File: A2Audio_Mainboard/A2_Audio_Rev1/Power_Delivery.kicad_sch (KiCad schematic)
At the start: 93 parts, among them J1 USB_C_Receptacle, U1 USBLC6-2SC6, U13 LT3042xMSE, U14 W25Q16JVSS, U19 TPS62130, U2 TPS65987DDHRSHR, U21 TPS61230DRC, U24 TPS65131RGE, U25 LT3094xDD, U3 TUSB546A-DCIRNQR, U4 BQ25895RTWR, U5 MAX17055ETB_T

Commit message: Added footprints and a few more parts.
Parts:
- C1, C19, C2, C20, C21, C22, C3, C38, C4, C42, C43, C44, C45, C47, C48, C49, C5, C50, C51, C52, C53, C54, C55, C56, C57, C6, C64, C65, C66, C67, C68, C69, C70, C71, C84, C85, C86, C87, C88, C89, C90, C92: footprint (none) -> Capacitor_SMD:C_0402_1005Metric
- D1: footprint (none) -> LED_SMD:LED_0603_1608Metric
- R1, R11, R12, R13, R14, R15, R16, R17, R18, R19, R2, R20, R21, R22, R23, R24, R25, R27, R28, R3, R31, R32, R33, R34, R35, R36, R4, R5, R6, R9: footprint (none) -> Resistor_SMD:R_0402_1005Metric
- TH1: footprint (none) -> Resistor_SMD:R_0603_1608Metric

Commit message: More Refinement
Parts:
- added J4: 12401610E4_2A, custom:AMPHENOL_12401610E4_2A, symbol 12401610E4_2A:12401610E4_2A
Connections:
- net CC1: now also J4.A5 (CC1)
- net CC2: now also J4.B5 (CC2)
- net D+1: now reaches J1.A6 (D+), J1.B6 (D+), U1.3 (I/O2)
- net D-1: now reaches J1.A7 (D-), J1.B7 (D-), U1.1 (I/O1)
- net TYPEC_RX1_N renamed RX1-1
- net TYPEC_RX1_P renamed RX1+1
- net VBUS_RAW renamed VBUS_A
- net VBUS_A: now also J4.A4 (VBUS_A), J4.A9 (VBUS_A), J4.B4 (VBUS_B), J4.B9 (VBUS_B)
- new net: J4.SH1 (SHIELD), J4.SH2 (SHIELD), J4.SH3 (SHIELD), J4.SH4 (SHIELD)
- new net GND_A: J4.A1 (GND_A), J4.A12 (GND_A)
- new net GND_B: J4.B1 (GND_B), J4.B12 (GND_B)

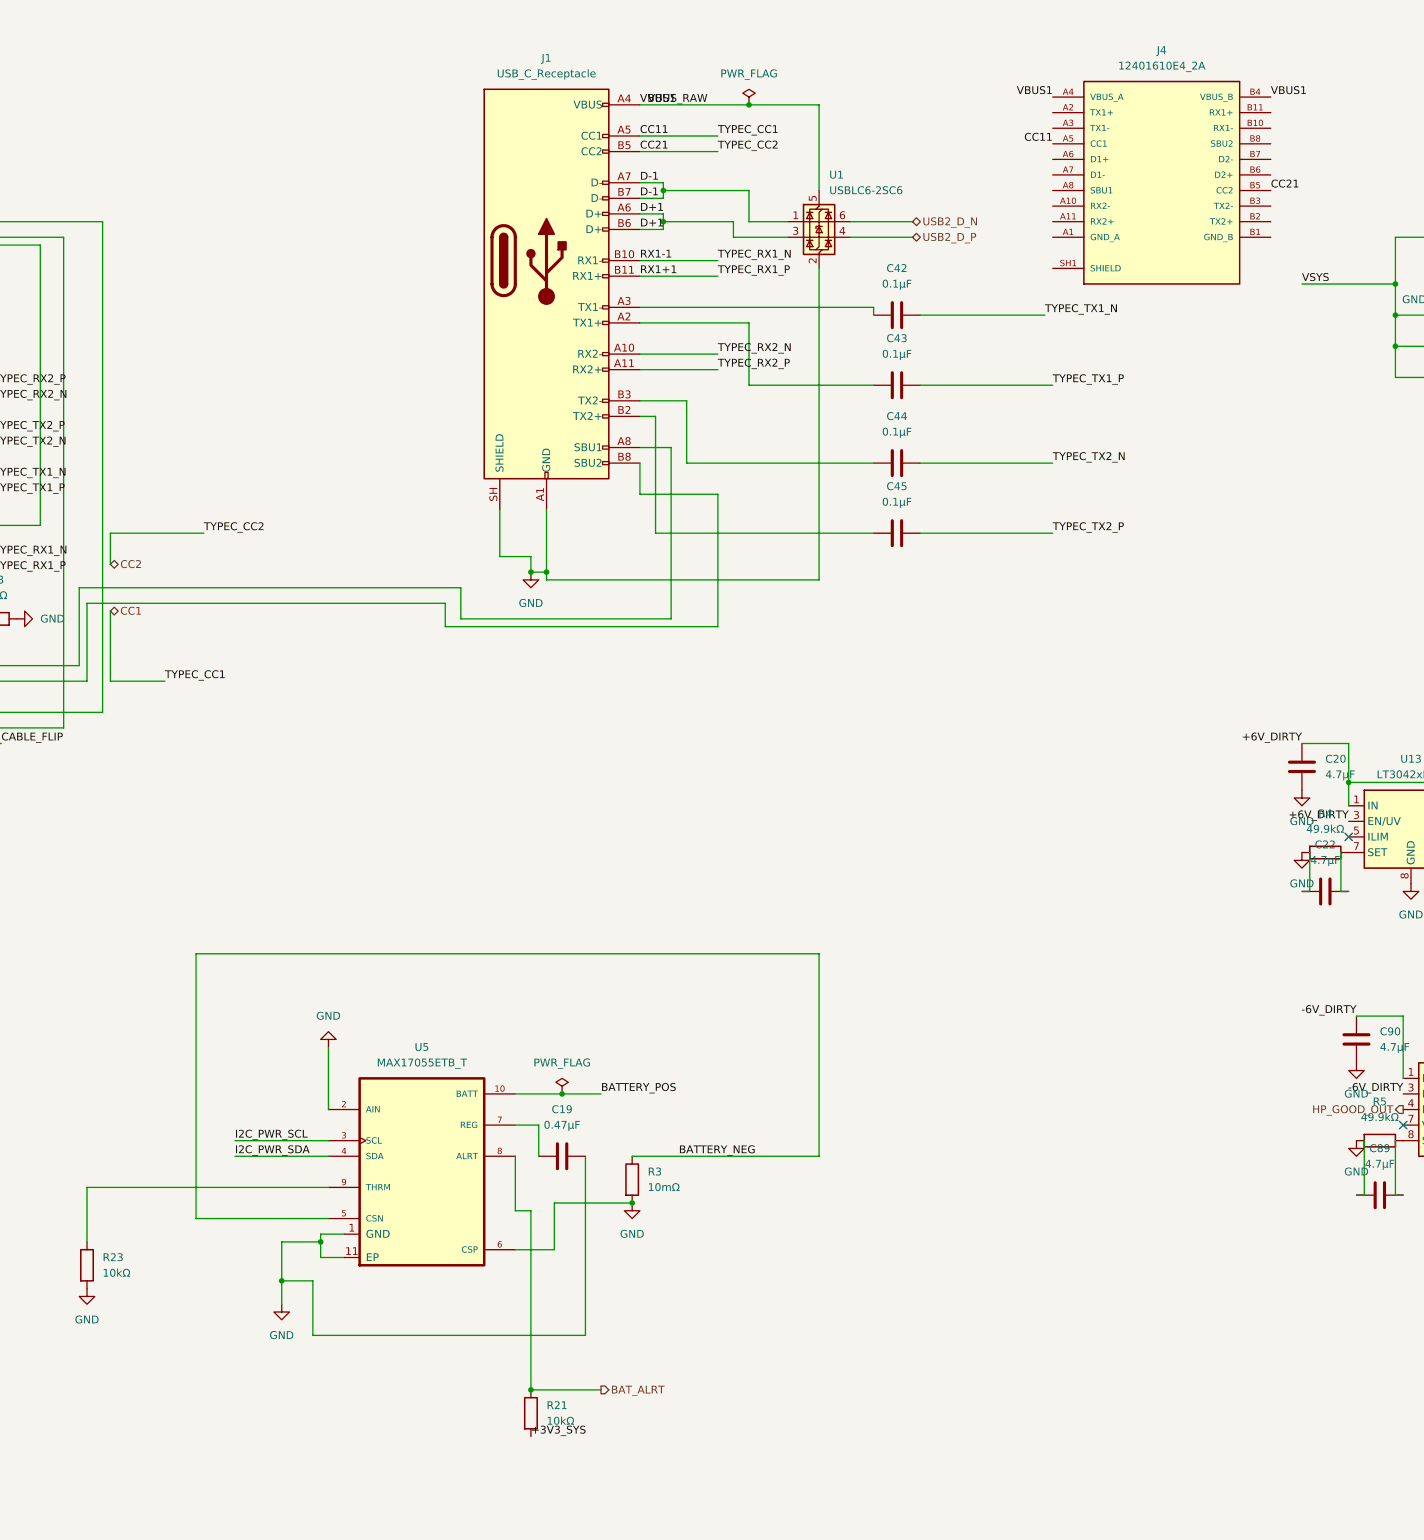
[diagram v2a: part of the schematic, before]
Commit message: Refining of logic and adding battery connector
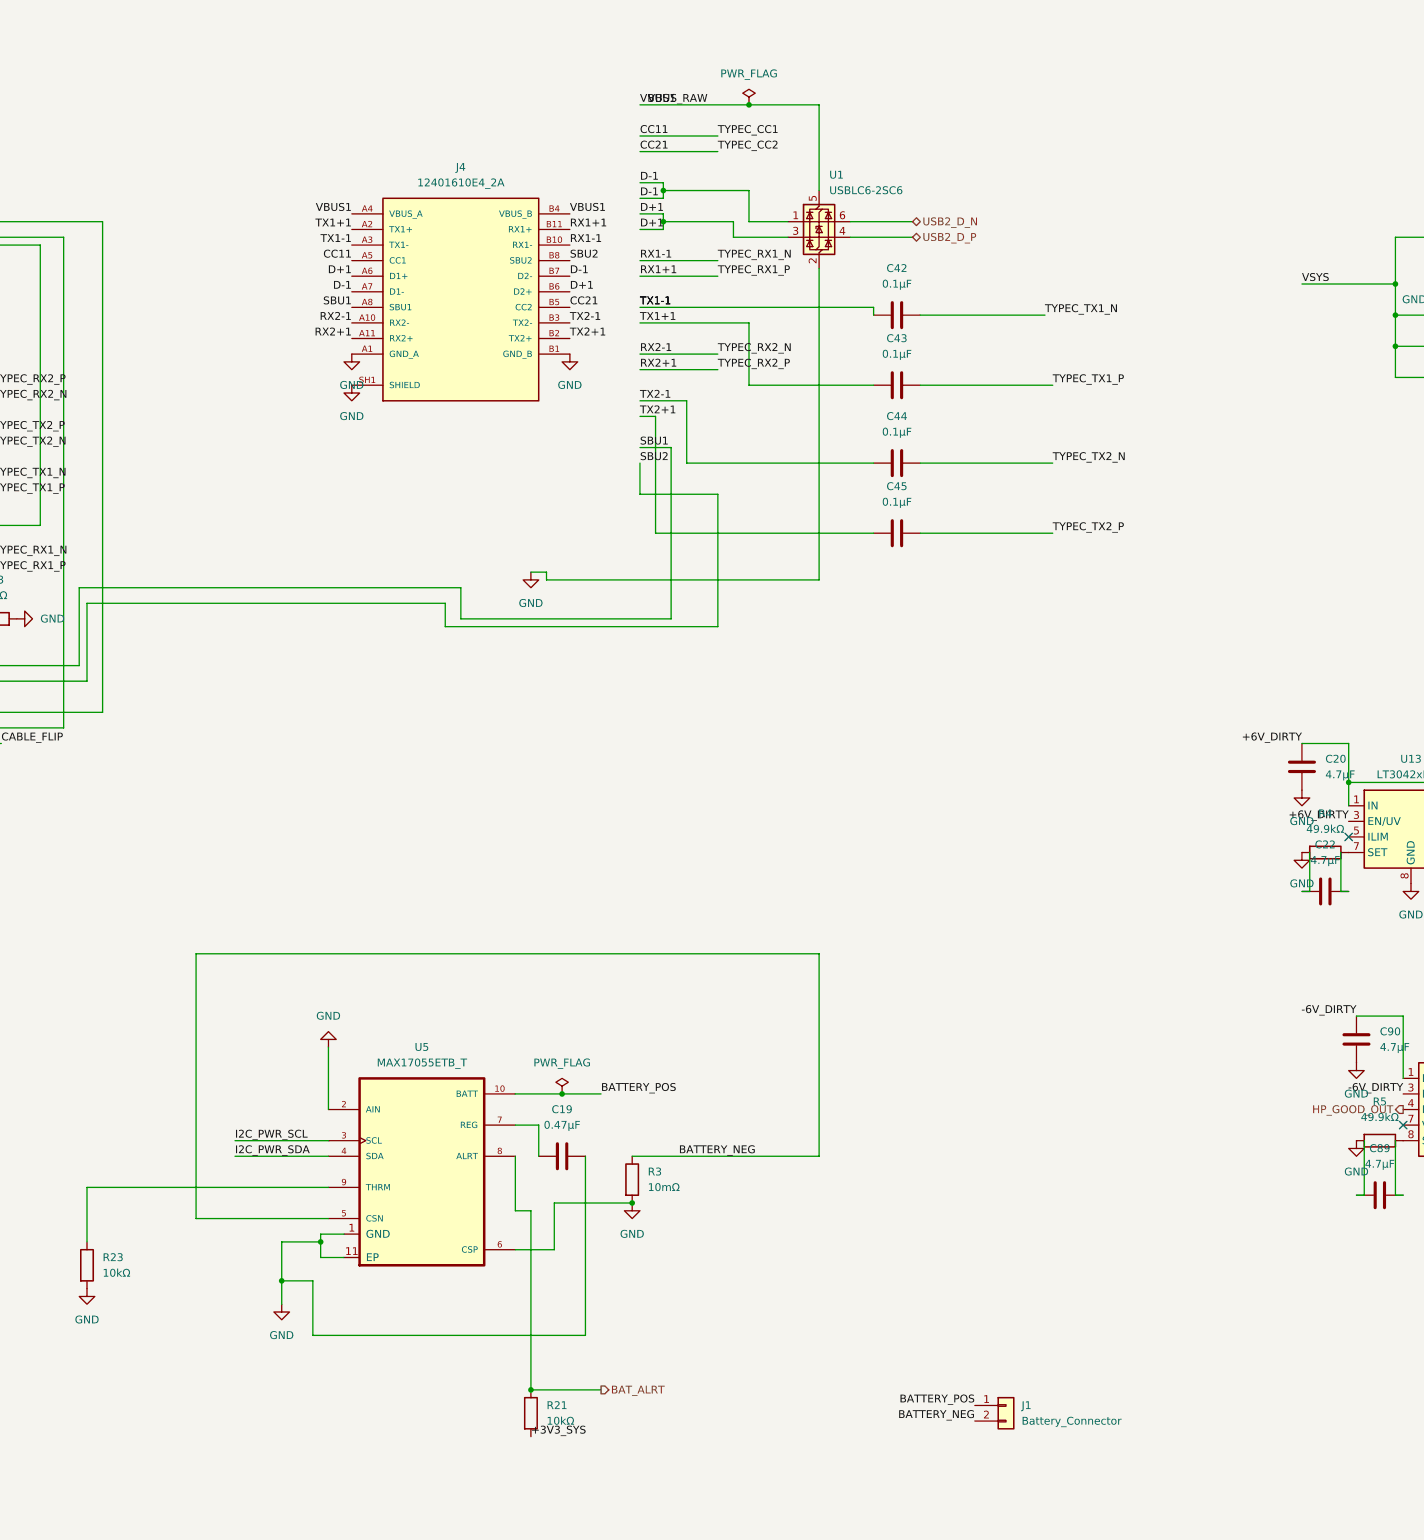
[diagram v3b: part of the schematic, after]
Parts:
- removed J1: USB_C_Receptacle, symbol symbols:USB_C_Receptacle
- added J1: Battery_Connector, Connector_JST:JST_PH_S2B-PH-K_1x02_P2.00mm_Horizontal, symbol symbols:Conn_01x02
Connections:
- net GND_A is gone; now on net CSP: J4.A1 (GND_A), J4.A12 (GND_A)
- net GND_B is gone; now on net CSP: J4.B1 (GND_B), J4.B12 (GND_B)
- net TYPEC_RX2_N is gone; now on net RX2-1: U3.39 (RX2N)
- net TYPEC_RX2_P is gone; now on net RX2+1: U3.40 (RX2P)
- net BAT: now also J1.1 (Pin_1)
- net BATTERY_NEG: now also J1.2 (Pin_2)
- net CSP: now also J4.SH1 (SHIELD), J4.SH2 (SHIELD), J4.SH3 (SHIELD), J4.SH4 (SHIELD)
- net D+1: now also J4.A6 (D1+), J4.B6 (D2+)
- net D-1: now also J4.A7 (D1-), J4.B7 (D2-)
- net RX1+1: now also J4.B11 (RX1+)
- net RX1-1: now also J4.B10 (RX1-)
- net TX2-1: now reaches C44.1
- net TX2-1: now also J4.B3 (TX2-)
- net RX2-1: now reaches J4.A10 (RX2-)
- net RX2+1: now reaches J4.A11 (RX2+)
- net TX1+1: now reaches J4.A2 (TX1+)
- net TX1+1: now also C43.1
- net TX1-1: now reaches J4.A3 (TX1-)
- net TX1-1: now also C42.1
- net SBU1: now reaches J4.A8 (SBU1)
- net SBU1: now also U3.27 (SBU1)
- net TX2+1: now reaches J4.B2 (TX2+)
- net TX2+1: now also C45.1
- net SBU2: now reaches J4.B8 (SBU2)
- net SBU2: now also U3.26 (SBU2)
- net CC1 renamed CC11
- net CC2 renamed CC21
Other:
- moved on the sheet: J4

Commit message: Fixing ERC errors
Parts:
- removed C64, C65, C66, C67, C68, C69, C70, C71: 100nF, Capacitor_SMD:C_0402_1005Metric, symbol symbols:C
- removed C85: 22µF, Capacitor_SMD:C_0402_1005Metric, symbol symbols:C
- removed C86: 0.22µF, Capacitor_SMD:C_0402_1005Metric, symbol symbols:C
- removed R19: 100kΩ, Resistor_SMD:R_0402_1005Metric, symbol symbols:R
- removed R31: 1MΩ, Resistor_SMD:R_0402_1005Metric, symbol symbols:R
- removed R32: 255kΩ, Resistor_SMD:R_0402_1005Metric, symbol symbols:R
- removed U24: TPS65131RGE, Package_DFN_QFN:VQFN-24-1EP_4x4mm_P0.5mm_EP2.45x2.45mm_ThermalVias, symbol symbols:TPS65131RGE
- added C111: 4.7µF, Capacitor_SMD:C_0402_1005Metric, symbol symbols:C
- added C112: 0.1µF, Capacitor_SMD:C_0402_1005Metric, symbol symbols:C
- added C113: 1µF, Capacitor_SMD:C_0402_1005Metric, symbol symbols:C
- added R55: 205kΩ, Resistor_SMD:R_0402_1005Metric, symbol symbols:R
- added U27: TPS65131RGE, Package_DFN_QFN:VQFN-24-1EP_4x4mm_P0.5mm_EP2.45x2.45mm_ThermalVias, symbol symbols:TPS65131RGE
- C84: value 22µF -> 4.7µF
- C87: value 4.7nF -> 0.1µF
- C88: value 4.7nF -> 4.7µF
- R28: value 316kΩ -> 23.7kΩ
- R34: value 205kΩ -> 806kΩ
- R36: value 100kΩ -> 806kΩ
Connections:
- net +3V3_SYS: now also U14.3 (~{WP}/IO_{2})
- net +6V_DIRTY: now also C87.1, R36.2, U27.23 (VPOS)
- net -6V_DIRTY: now also R34.2, U25.5 (PGFB), U25.7 (VIOC), C111.1, C112.1, U27.15 (VNEG); no longer R34.1
- net CSP: now also C22.2, C89.2, L6.2, R20.2, R35.1, C111.2, C112.2, C113.2, R55.1, U27.19 (AGND), U27.2 (PGND), U27.25 (EP), U27.3 (PGND); no longer C88.2, L6.1
- net DP_LANE0_N: now also U3.10 (DP0N)
- net DP_LANE0_P: now also U3.9 (DP0P)
- net DP_LANE1_N: now also U3.13 (DP1N)
- net DP_LANE1_P: now also U3.12 (DP1P)
- net DP_LANE2_N: now also U3.16 (DP2N)
- net DP_LANE2_P: now also U3.15 (DP2P)
- net DP_LANE3_N: now also U3.19 (DP3N)
- net DP_LANE3_P: now also U3.18 (DP3P)
- net SYS: now also U27.1 (INP), U27.10 (ENN), U27.11 (PSN), U27.24 (INP), U27.4 (VIN), U27.5 (INN), U27.6 (INN), U27.8 (ENP), U27.9 (PSP)
- net VBUS_A: no longer U2.15 (DRAIN1), U2.19 (DRAIN1), U2.52 (DRAIN2), U2.56 (DRAIN2), U2.57 (DRAIN2), U2.57_1 (DRAIN2), U2.57_2 (DRAIN2), U2.57_3 (DRAIN2), U2.57_4 (DRAIN2), U2.57_5 (DRAIN2), U2.57_6 (DRAIN2), U2.58 (DRAIN1), U2.58_1 (DRAIN1), U2.58_2 (DRAIN1), U2.58_3 (DRAIN1), U2.58_4 (DRAIN1), U2.58_5 (DRAIN1), U2.58_6 (DRAIN1), U2.7 (DRAIN2), U2.8 (DRAIN1)
- net VBUS_PD: now also U2.15 (DRAIN1), U2.19 (DRAIN1), U2.52 (DRAIN2), U2.56 (DRAIN2), U2.57 (DRAIN2), U2.57_1 (DRAIN2), U2.57_2 (DRAIN2), U2.57_3 (DRAIN2), U2.57_4 (DRAIN2), U2.57_5 (DRAIN2), U2.57_6 (DRAIN2), U2.58 (DRAIN1), U2.58_1 (DRAIN1), U2.58_2 (DRAIN1), U2.58_3 (DRAIN1), U2.58_4 (DRAIN1), U2.58_5 (DRAIN1), U2.58_6 (DRAIN1), U2.7 (DRAIN2), U2.8 (DRAIN1)
- net at R36.1: now also R55.2, U27.22 (FBP)
- net at C88.1: now also U27.18 (CN); no longer R36.2
- net at R35.2: now also R20.1, U2.10 (ADCIN2); no longer C87.1
- net at C38.2, R1.1, R18.1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: no longer R20.2, U14.3 (~{WP}/IO_{2})
- net at R5.1, U25.8 (SET): now also C89.1
- net at R4.1, U13.7 (SET): now also C22.1
- net at D4.1 (K): now also L6.1, U27.13 (OUTN), U27.14 (OUTN); no longer L6.2
- net at R33.2: now also R34.1, U27.16 (FBN); no longer R34.2
- net at R33.1: now also C113.1, U27.17 (VREF)
- net at D3.2 (A), L5.2: now also U27.7 (BSW)
- new net: C88.2, U27.21 (CP)
- no-connect marks 25 -> 22
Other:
- moved on the sheet: C20, C21, C22, C84, C88, C89, C90, C92, D3, D4, L5, R33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

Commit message: Fixed even more schematic errors
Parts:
- R24: value 130Ω -> 180Ω
- R36: value 806kΩ -> 10kΩ
- R55: value 205kΩ -> 31.6kΩ
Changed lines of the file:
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@@
 			)
 		)
-		(property "Value" "806kΩ"
+		(property "Value" "10kΩ"
 			(at 524.51 66.04 90)
 			(show_name no)
@@
 			)
 		)
-		(property "Value" "130Ω"
+		(property "Value" "180Ω"
 			(at 49.53 289.56 90)
 			(show_name no)
@@
 		(in_pos_files yes)
 		(dnp no)
-		(fields_autoplaced yes)
 		(property "Reference" "R55"
 			(at 524.51 58.42 90)
@@
 			)
 		)
-		(property "Value" "205kΩ"
+		(property "Value" "31.6kΩ"
 			(at 524.51 60.96 90)
 			(show_name no)

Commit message: Fixed SD Card logic and power error
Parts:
- removed C54: 10nF, Capacitor_SMD:C_0402_1005Metric, symbol symbols:C
- removed C55, C57: 22µF, Capacitor_SMD:C_0402_1005Metric, symbol symbols:C
- removed C56: 0.1µF, Capacitor_SMD:C_0402_1005Metric, symbol symbols:C
- removed L4: 1.0µH, symbol symbols:L
- removed U21: TPS61230DRC, Package_SON:Texas_S-PVSON-N10_ThermalVias, symbol symbols:TPS61230DRC
- added C114, C65, C67: 0.1µF, Capacitor_SMD:C_0402_1005Metric, symbol symbols:C
- added C16: 10µF, Capacitor_SMD:C_0603_1608Metric, symbol symbols:C
- added C66: 10µF, Capacitor_SMD:C_0402_1005Metric, symbol symbols:C
- added C68: 47nF, Capacitor_SMD:C_0603_1608Metric, symbol symbols:C
- added C69: 4.7nF, Capacitor_SMD:C_0402_1005Metric, symbol symbols:C
- added C70: 220pF, Capacitor_SMD:C_0402_1005Metric, symbol symbols:C
- added C71: 1µF, Capacitor_SMD:C_0402_1005Metric, symbol symbols:C
- added C85, C86: 22µF, Capacitor_SMD:C_0603_1608Metric, symbol symbols:C
- added L7: 1.0µH, Inductor_SMD:L_Bourns_SRP5030T, symbol symbols:L
- added R58, R59: 100kΩ, Resistor_SMD:R_0402_1005Metric, symbol symbols:R
- added R60: 120kΩ, Resistor_SMD:R_0402_1005Metric, symbol symbols:R
- added R61: 15kΩ, Resistor_SMD:R_0402_1005Metric, symbol symbols:R
- added R62: 10kΩ, Resistor_SMD:R_0402_1005Metric, symbol symbols:R
- added U17: TPS61088RHLR, TPS61088RHLR:IC_TPS61088RHLR, symbol TPS61088RHLR:TPS61088RHLR
- C2, C3, C47, C48: footprint Capacitor_SMD:C_0402_1005Metric -> Capacitor_SMD:C_0603_1608Metric
- C92: value 4.7µF -> 22µF; footprint Capacitor_SMD:C_0402_1005Metric -> Capacitor_SMD:C_0805_2012Metric
- L1, L3: footprint (none) -> Inductor_SMD:L_Bourns_SRP5030T
- L5, L6: footprint (none) -> Inductor_SMD:L_0805_2012Metric
- R27: value 100kΩ -> 316kΩ; footprint Resistor_SMD:R_0402_1005Metric -> (none)
- R28: value 23.7kΩ -> 100kΩ; footprint Resistor_SMD:R_0402_1005Metric -> (none)
- R3: footprint Resistor_SMD:R_0402_1005Metric -> Resistor_SMD:R_2010_5025Metric
- R34: value 806kΩ -> 1.0MΩ
- R36: value 10kΩ -> 124kΩ
- R4, R5: value 49.9kΩ -> 45.3kΩ
- R9: value R -> 1kΩ
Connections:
- net +3V3_SYS: now also R58.2; no longer R21.2, R22.2, R25.2, R6.2, U14.3 (~{WP}/IO_{2})
- net +5V_CM5: now also R27.2, C114.1, C85.1, C86.1, U17.14 (VOUT_16), U17.15 (VOUT_14), U17.16 (VOUT_15); no longer R28.1
- net CSP: now also R28.2, C114.2, C16.2, C65.2, C66.2, C68.2, C69.2, C70.1, C71.1, C71.2, C85.2, C86.2, R59.2, R60.1, R61.2, U17.1 (VCC), U17.13 (MODE), U17.20 (AGND), U17.21 (PGND), U17.22 (PGND), U17.23 (PGND), U17.24 (PGND), U17.25 (PGND), U17.26 (PGND), U17.27 (PGND), U17.28 (PGND), U17.29 (PGND); no longer R27.2
- net DP_AUX_N: now also R58.1
- net DP_AUX_P: now also R59.1
- net SYS: now also C65.1, C66.1, L7.2, U17.2 (EN), U17.9 (VIN)
- net at C38.2, R1.1, R18.1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: now also U14.3 (~{WP}/IO_{2}), C16.1
- net at R27.1: now also R28.1, U17.17 (FB); no longer R28.2
- new net: R60.2, U17.3 (FSW)
- new net: C70.2, R62.1, U17.18 (COMP)
- new net: C69.1, R62.2
- new net: C68.1, U17.10 (SS)
- new net: R61.1, U17.19 (ILIM)
- new net: C67.2, L7.1, U17.4 (SW_7), U17.5 (SW_4), U17.6 (SW_5), U17.7 (SW_6)
- new net: C67.1, U17.8 (BOOT)
- new net +3V3_SYSPI: R21.2, R22.2, R25.2, R6.2
- no-connect marks 22 -> 20
